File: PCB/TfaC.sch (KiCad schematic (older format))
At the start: 1 part, among them P101 Line

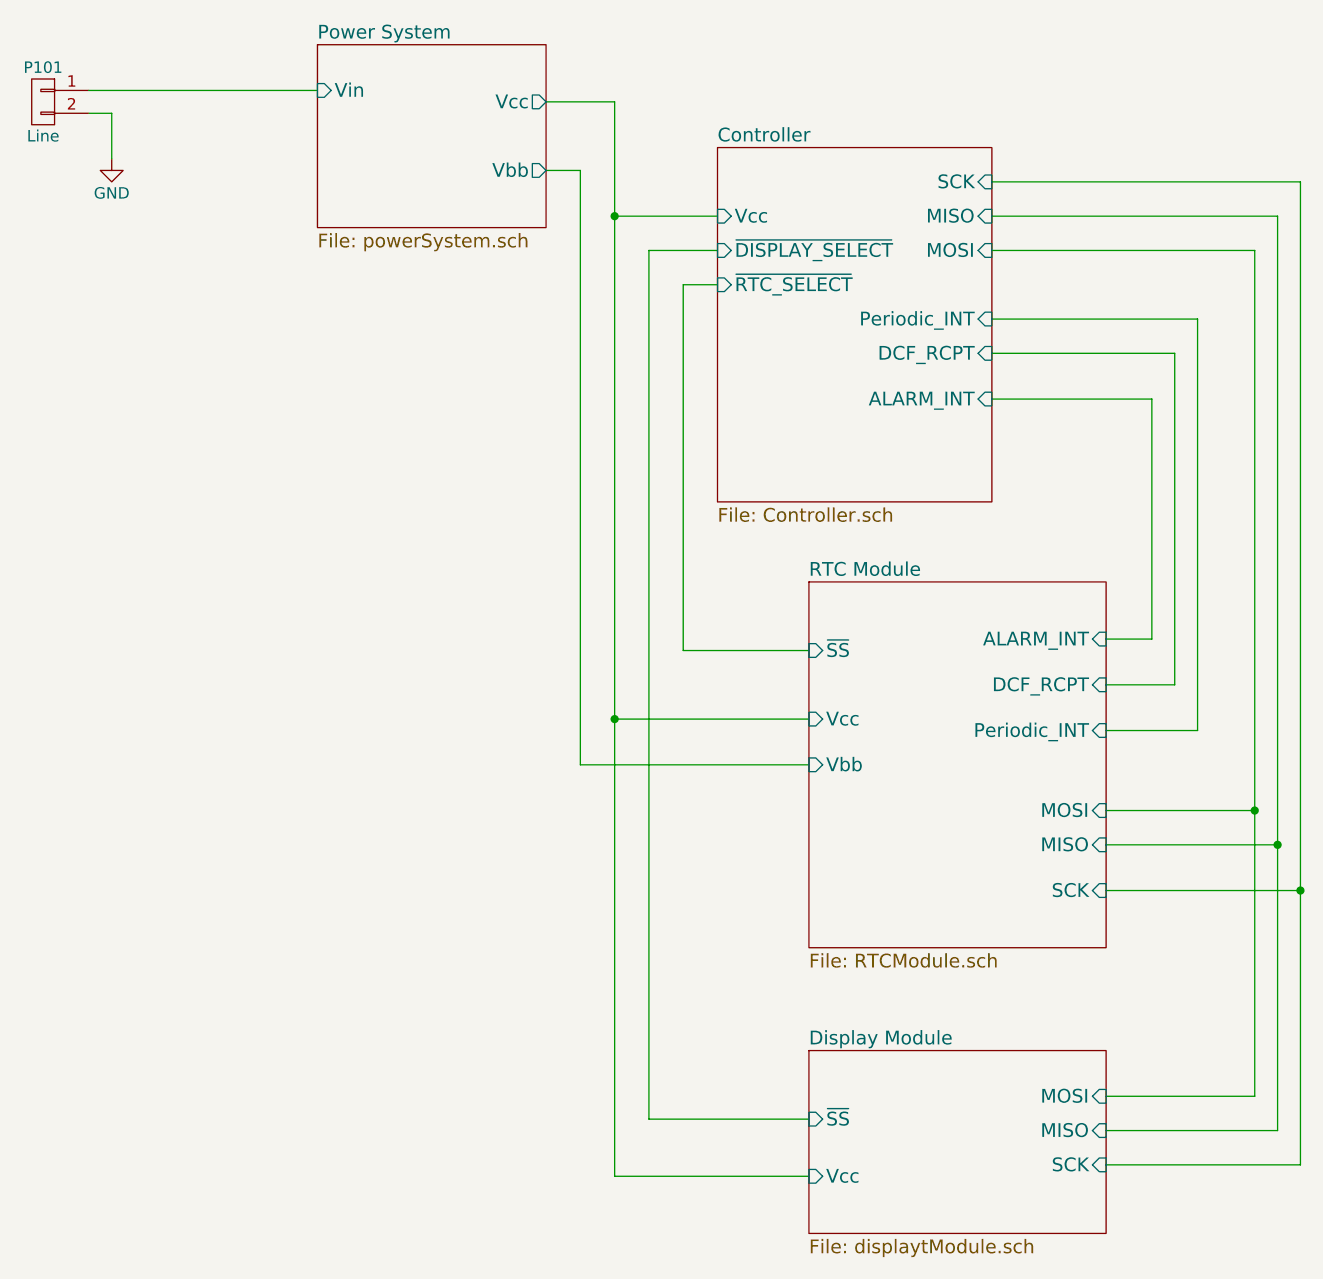
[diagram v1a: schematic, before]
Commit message: Updated the board for further features to the display
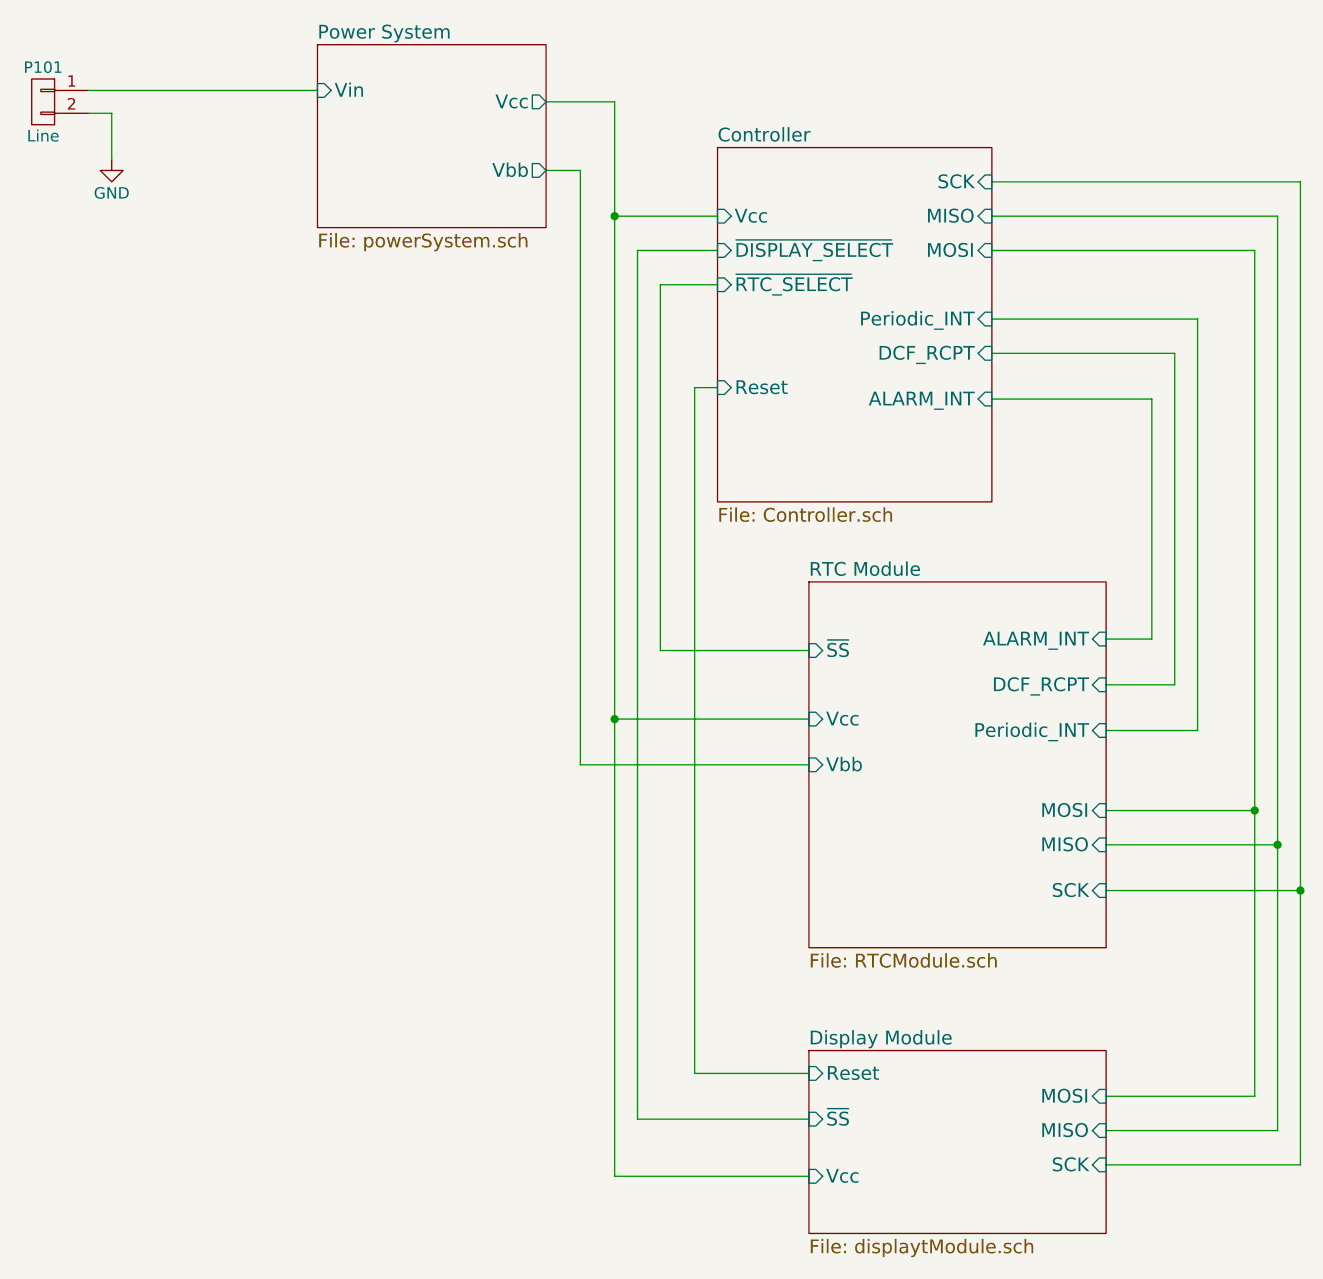
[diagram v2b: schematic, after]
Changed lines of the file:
@@
 F5 "SCK" I R 5850 5750 60
 F6 "Vcc" I L 4550 5800 60
+F7 "Reset" I L 4550 5350 60
 $EndSheet
 $Sheet
@@
 F9 "DCF_RCPT" I R 5350 2200 60
 F10 "ALARM_INT" I R 5350 2400 60
+F11 "Reset" I L 4150 2350 60
 $EndSheet
 Wire Wire Line
@@
 Connection ~ 3700 3800
 Wire Wire Line
-	4150 1750 3850 1750
+	4150 1750 3800 1750
 Wire Wire Line
-	3850 1750 3850 5550
+	3800 1750 3800 5550
 Wire Wire Line
-	3850 5550 4550 5550
+	3800 5550 4550 5550
 Wire Wire Line
-	4150 1900 4000 1900
+	4150 1900 3900 1900
 Wire Wire Line
-	4000 1900 4000 3500
+	3900 1900 3900 3500
 Wire Wire Line
-	4000 3500 4550 3500
+	3900 3500 4550 3500
 Wire Wire Line
 	6500 1750 6500 5450
@@
 Wire Wire Line
 	5350 1750 6500 1750
+Wire Wire Line
+	4150 2350 4050 2350
+Wire Wire Line
+	4050 2350 4050 5350
+Wire Wire Line
+	4050 5350 4550 5350
 $EndSCHEMATC
